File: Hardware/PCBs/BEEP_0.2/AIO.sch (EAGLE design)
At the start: 83 parts, among them IC1 ULN2803ASOP18, IC2 ULN2803ASOP18, IC3 74HC238SSOP, IC4 74HC238SSOP, IC5 TS34119SMD, U2 TB6612FNG, U3 ATXMEGA64D3-AU, X1 MICROMATCH-4, X10 MICROMATCH-10, X3 MICROMATCH-8, X4 MICROMATCH-8, X5 MICROMATCH-8, X8 MICROMATCH-8, X9 MICROMATCH-4

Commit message: add poweroff line to atxmega
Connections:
- removed net N$18: R8.2, S1.S, S1.S1, U$7.G1
- new net POWER_OFF: R8.2, S1.S, S1.S1, U$7.G1, U3.PC7
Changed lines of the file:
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@@
 </segment>
 </net>
-<net name="N$18" class="0">
+<net name="POWER_OFF" class="0">
 <segment>
 <pinref part="R8" gate="G$1" pin="2"/>
@@
 <wire x1="492.76" y1="287.02" x2="492.76" y2="284.48" width="0.1524" layer="91"/>
 <junction x="492.76" y="284.48"/>
+<wire x1="497.84" y1="299.72" x2="502.92" y2="299.72" width="0.1524" layer="91"/>
+<label x="502.92" y="299.72" size="1.778" layer="95" xref="yes"/>
+</segment>
+<segment>
+<pinref part="U3" gate="G$1" pin="PC7"/>
+<wire x1="129.54" y1="96.52" x2="134.62" y2="96.52" width="0.1524" layer="91"/>
+<label x="134.62" y="96.52" size="1.27" layer="95" xref="yes"/>
 </segment>
 </net>

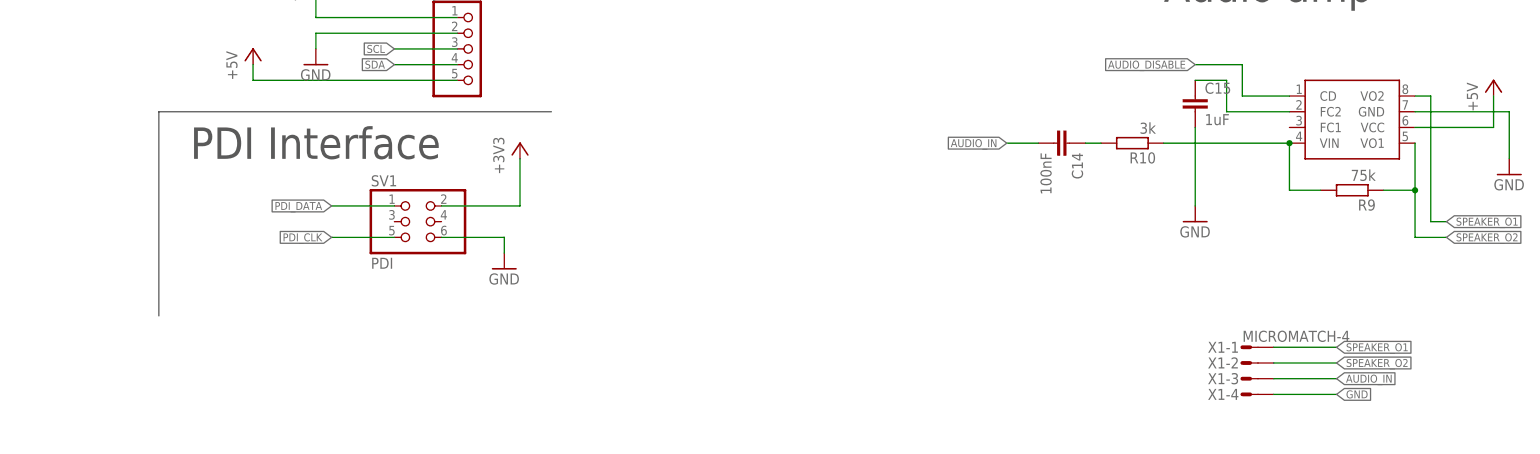
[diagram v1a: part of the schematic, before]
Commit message: move folders try to apply drc from sparkfun (wip) moved audio connetor add slice for camera flexcable
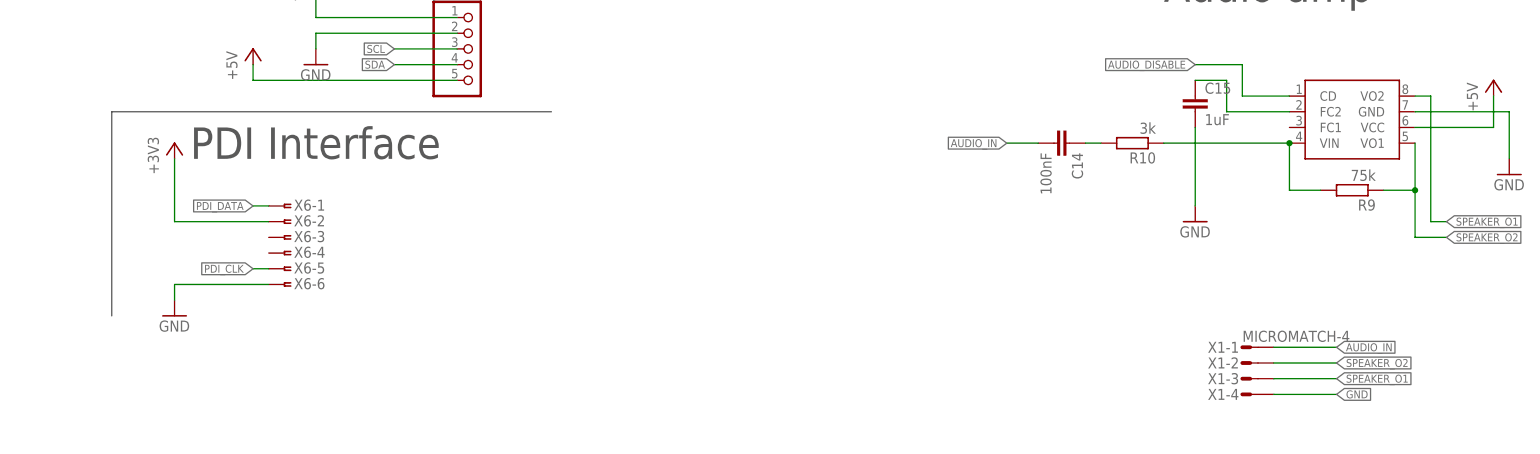
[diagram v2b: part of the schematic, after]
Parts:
- removed SV1: PDI, pinhead:PINHD-2X3
- added X6: (no value), con-amp:FTOP-6
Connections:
- net +3V3: now also X6-2.1; no longer SV1.2
- net AUDIO_IN: now also X1-1.S; no longer X1-3.S
- net GND: now also X6-6.1; no longer SV1.6
- net PDI_CLK: now also X6-5.1; no longer SV1.5
- net PDI_DATA: now also X6-1.1; no longer SV1.1
- net SPEAKER_O1: now also X1-3.S; no longer X1-1.S
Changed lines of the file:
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@@
 <part name="+3V18" library="supply1" deviceset="+3V3" device=""/>
 <part name="+3V19" library="supply1" deviceset="+3V3" device=""/>
-<part name="SV1" library="pinhead" deviceset="PINHD-2X3" device="" value="PDI"/>
-<part name="+3V20" library="supply1" deviceset="+3V3" device=""/>
-<part name="GND37" library="supply1" deviceset="GND" device=""/>
 <part name="+3V21" library="supply1" deviceset="+3V3" device=""/>
 <part name="R34" library="rcl" deviceset="R-EU_" device="R0603" value="10K"/>
@@
 <part name="X1" library="Con-amp-micromatch" deviceset="MICROMATCH-4" device=""/>
 <part name="X2" library="con-amp" deviceset="FSIDE-8" device=""/>
+<part name="X6" library="con-amp" deviceset="FTOP-6" device=""/>
+<part name="+3V8" library="supply1" deviceset="+3V3" device=""/>
+<part name="GND46" library="supply1" deviceset="GND" device=""/>
 </parts>
 <sheets>
@@
 <text x="119.38" y="411.48" size="5.08" layer="97">RGB LEDs &amp; IR distance sensors</text>
 <wire x1="457.2" y1="111.76" x2="457.2" y2="30.48" width="0.1524" layer="97"/>
-<wire x1="269.24" y1="83.82" x2="205.74" y2="83.82" width="0.1524" layer="97"/>
-<wire x1="205.74" y1="83.82" x2="205.74" y2="50.8" width="0.1524" layer="97"/>
+<wire x1="269.24" y1="83.82" x2="198.12" y2="83.82" width="0.1524" layer="97"/>
+<wire x1="198.12" y1="83.82" x2="198.12" y2="50.8" width="0.1524" layer="97"/>
 <text x="210.82" y="76.2" size="5.08" layer="97">PDI Interface</text>
 <wire x1="269.24" y1="127" x2="269.24" y2="124.46" width="0.1524" layer="97"/>
@@
 <instance part="+3V18" gate="G$1" x="215.9" y="187.96"/>
 <instance part="+3V19" gate="G$1" x="220.98" y="187.96"/>
-<instance part="SV1" gate="A" x="246.38" y="66.04"/>
-<instance part="+3V20" gate="G$1" x="264.16" y="78.74"/>
-<instance part="GND37" gate="1" x="261.62" y="58.42"/>
 <instance part="+3V21" gate="G$1" x="86.36" y="182.88"/>
 <instance part="R34" gate="G$1" x="86.36" y="170.18" rot="R270"/>
@@
 <instance part="X2" gate="-7" x="228.6" y="345.44"/>
 <instance part="X2" gate="-8" x="228.6" y="342.9"/>
+<instance part="X6" gate="-1" x="226.06" y="68.58"/>
+<instance part="X6" gate="-2" x="226.06" y="66.04"/>
+<instance part="X6" gate="-3" x="226.06" y="63.5"/>
+<instance part="X6" gate="-4" x="226.06" y="60.96"/>
+<instance part="X6" gate="-5" x="226.06" y="58.42"/>
+<instance part="X6" gate="-6" x="226.06" y="55.88"/>
+<instance part="+3V8" gate="G$1" x="208.28" y="78.74"/>
+<instance part="GND46" gate="1" x="208.28" y="50.8"/>
 </instances>
 <busses>
@@
 <wire x1="238.76" y1="165.1" x2="228.6" y2="165.1" width="0.1524" layer="91"/>
 <wire x1="228.6" y1="165.1" x2="228.6" y2="154.94" width="0.1524" layer="91"/>
-</segment>
-<segment>
-<pinref part="SV1" gate="A" pin="6"/>
-<pinref part="GND37" gate="1" pin="GND"/>
-<wire x1="251.46" y1="63.5" x2="261.62" y2="63.5" width="0.1524" layer="91"/>
-<wire x1="261.62" y1="63.5" x2="261.62" y2="60.96" width="0.1524" layer="91"/>
 </segment>
 <segment>
@@
 <wire x1="386.08" y1="38.1" x2="396.24" y2="38.1" width="0.1524" layer="91"/>
 <label x="396.24" y="38.1" size="1.27" layer="95" xref="yes"/>
+</segment>
+<segment>
+<pinref part="GND46" gate="1" pin="GND"/>
+<wire x1="223.52" y1="55.88" x2="208.28" y2="55.88" width="0.1524" layer="91"/>
+<wire x1="208.28" y1="55.88" x2="208.28" y2="53.34" width="0.1524" layer="91"/>
+<pinref part="X6" gate="-6" pin="1"/>
 </segment>
 </net>
@@
 </segment>
 <segment>
-<pinref part="SV1" gate="A" pin="2"/>
-<pinref part="+3V20" gate="G$1" pin="+3V3"/>
-<wire x1="251.46" y1="68.58" x2="264.16" y2="68.58" width="0.1524" layer="91"/>
-<wire x1="264.16" y1="68.58" x2="264.16" y2="76.2" width="0.1524" layer="91"/>
-</segment>
-<segment>
 <pinref part="R34" gate="G$1" pin="1"/>
 <pinref part="+3V21" gate="G$1" pin="+3V3"/>
@@
 <wire x1="254" y1="99.06" x2="231.14" y2="99.06" width="0.1524" layer="91"/>
 <wire x1="231.14" y1="99.06" x2="231.14" y2="104.14" width="0.1524" layer="91"/>
+</segment>
+<segment>
+<pinref part="+3V8" gate="G$1" pin="+3V3"/>
+<wire x1="223.52" y1="66.04" x2="208.28" y2="66.04" width="0.1524" layer="91"/>
+<wire x1="208.28" y1="66.04" x2="208.28" y2="76.2" width="0.1524" layer="91"/>
+<pinref part="X6" gate="-2" pin="1"/>
 </segment>
 </net>
@@
 <net name="PDI_DATA" class="0">
 <segment>
-<pinref part="SV1" gate="A" pin="1"/>
-<wire x1="243.84" y1="68.58" x2="233.68" y2="68.58" width="0.1524" layer="91"/>
-<label x="233.68" y="68.58" size="1.27" layer="95" rot="R180" xref="yes"/>
-</segment>
-<segment>
 <wire x1="93.98" y1="157.48" x2="78.74" y2="157.48" width="0.1524" layer="91"/>
 <label x="78.74" y="157.48" size="1.27" layer="95" rot="R180" xref="yes"/>
 <pinref part="U3" gate="G$1" pin="PDI"/>
 </segment>
+<segment>
+<label x="220.98" y="68.58" size="1.27" layer="95" rot="R180" xref="yes"/>
+<pinref part="X6" gate="-1" pin="1"/>
+<wire x1="220.98" y1="68.58" x2="223.52" y2="68.58" width="0.1524" layer="91"/>
+</segment>
 </net>
 <net name="PDI_CLK" class="0">
-<segment>
-<pinref part="SV1" gate="A" pin="5"/>
-<wire x1="243.84" y1="63.5" x2="233.68" y2="63.5" width="0.1524" layer="91"/>
-<label x="233.68" y="63.5" size="1.27" layer="95" rot="R180" xref="yes"/>
-</segment>
 <segment>
 <wire x1="93.98" y1="160.02" x2="86.36" y2="160.02" width="0.1524" layer="91"/>
@@
 <junction x="86.36" y="160.02"/>
 <pinref part="U3" gate="G$1" pin="!RESET!/PDI"/>
+</segment>
+<segment>
+<label x="220.98" y="58.42" size="1.27" layer="95" rot="R180" xref="yes"/>
+<pinref part="X6" gate="-5" pin="1"/>
+<wire x1="220.98" y1="58.42" x2="223.52" y2="58.42" width="0.1524" layer="91"/>
 </segment>
 </net>
@@
 </segment>
 <segment>
-<wire x1="386.08" y1="40.64" x2="396.24" y2="40.64" width="0.1524" layer="91"/>
-<pinref part="X1" gate="-3" pin="S"/>
-<label x="396.24" y="40.64" size="1.27" layer="95" xref="yes"/>
+<wire x1="386.08" y1="45.72" x2="396.24" y2="45.72" width="0.1524" layer="91"/>
+<pinref part="X1" gate="-1" pin="S"/>
+<label x="396.24" y="45.72" size="1.27" layer="95" xref="yes"/>
 </segment>
 </net>
@@
 </segment>
 <segment>
-<wire x1="386.08" y1="45.72" x2="396.24" y2="45.72" width="0.1524" layer="91"/>
-<pinref part="X1" gate="-1" pin="S"/>
-<label x="396.24" y="45.72" size="1.27" layer="95" xref="yes"/>
-</segment>
-</net>
+<wire x1="386.08" y1="40.64" x2="396.24" y2="40.64" width="0.1524" layer="91"/>
+<pinref part="X1" gate="-3" pin="S"/>
+<label x="396.24" y="40.64" size="1.27" layer="95" xref="yes"/>
+</segment>
+</net>

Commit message: enhance routing, add external crystal, move components for Raspberry Pi
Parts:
- removed JP12: Step_Down_Conn, pinhead:PINHD-1X3
- removed R32, R33: (no value), rcl:R-EU_R0603
- removed R34: 10K, rcl:R-EU_R0603
- removed R35, R36, R37: 100R, rcl:R-EU_R0603
- removed U$25: GY-81, BEEP:GY-81
- removed U$26: RASPBERRY-PI, BEEP:RASPBERRY-PI
- removed X15: (no value), con-amp:FSIDE-8
- added C16, C17: 22pF, rcl:C-EUC0603
- added Q4, Q5: DMN2075U, BEEP:DMN2075U
- added Q6: 32Mhz, crystal:CRYSTALHC49S
- added R11: 10k, rcl:R-EU_R0603
- added R12: 220R, rcl:R-EU_R0603
- added R13: 390R, rcl:R-EU_R0603
- added R15, R16: (no value), rcl:R-EU_R0603
- added R17: 3k, rcl:R-EU_R0603
- added R18: 75k, rcl:R-EU_R0603
- added X12, X13: MICROMATCH-4, Con-amp-micromatch:MICROMATCH-4
- C10: value 100nF -> 1uF
- C11, C12: value 100nF -> 10uF; device rcl:C-EUC0603 -> rcl:CPOL-EUSMCD
- C13: value 1uF -> 100nF
- C2, C4: value 10uF -> 100nF; device rcl:CPOL-EUSMCD -> rcl:C-EUC0603
- IC1, IC2: value ULN2803ASOP18 -> 74HC238SSOP; device BEEP:ULN2803ASOP18 -> BEEP:74HC238SSOP
- IC3, IC4: value 74HC238SSOP -> ULN2803ASOP18; device BEEP:74HC238SSOP -> BEEP:ULN2803ASOP18
- JP1: value (none) -> Step_Down_Conn; device pinhead:PINHD-1X5 -> pinhead:PINHD-1X3
- LED1: value (none) -> YELLOW
- LED2: value (none) -> RED
- LED3: value (none) -> blue
- R1, R2, R3: value (none) -> 100R
- R10: value 3k -> 10k
- R19: value (none) -> 1K
- R20, R24: value (none) -> 10k
- R21: value (none) -> 100k
- R22, R23, R25, R26, R27, R28, R29, R30: device rcl:R-EU_R0603 -> rcl:R-EU_R0805
- R31: value (none) -> 0R
- R4, R5: value 10K -> (none); device rcl:R-EU_R0603 -> rcl:R-EU_R0805
- R6: value 10k -> (none); device rcl:R-EU_R0603 -> rcl:R-EU_R0805
- R7: value 100k -> 10K
- R8: value 10k -> (none)
- R9: value 75k -> (none)
- S1: value (none) -> On / Off
- U$5: value DMN2075U -> GY-81; device BEEP:DMN2075U -> BEEP:GY-81
- U$7: value DMC3028LSD -> RASPBERRY-PI; device BEEP:DMC3028LSD -> BEEP:RASPBERRY-PI
- U$8: value DMN2075U -> DMC3028LSD; device BEEP:DMN2075U -> BEEP:DMC3028LSD
- X1: value MICROMATCH-4 -> Sens1; device Con-amp-micromatch:MICROMATCH-4 -> con-amp:FSIDE-8
- X10: value MICROMATCH-10 -> exp header; device Con-amp-micromatch:MICROMATCH-10 -> con-amp:FTOP-6
- X11: value (none) -> MICROMATCH-10; device con-amp:FSIDE-8 -> Con-amp-micromatch:MICROMATCH-10
- X2: value (none) -> Sens2
- X5: value MICROMATCH-8 -> PDI interface (ISP); device Con-amp-micromatch:MICROMATCH-8 -> con-amp:FTOP-6
- X6: value (none) -> Sens5; device con-amp:FTOP-6 -> con-amp:FSIDE-8
- X7: value (none) -> Sens6
- X9: value MICROMATCH-4 -> MICROMATCH-8; device Con-amp-micromatch:MICROMATCH-4 -> Con-amp-micromatch:MICROMATCH-8
- renumbered JP13 to JP2, LED10 to LED1, LED11 to LED3, LED9 to LED2, R41 to R14, R42 to R19, U$1 to Q3, U$2 to Q2, U$21 to U$9, U$22 to U$11, U$23 to U$10, U$24 to U$12, U$3 to Q1, U3 to U1, X16 to X7
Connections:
- new net N$14: C17.2, Q6.1, U1.PR1
- new net N$18: C16.2, Q6.2, U1.PR0
- net +3V3: now also C11.-, C13.2, C2.2, C3.2, C4.2, IC1.G1, IC1.VCC, IC2.G1, IC2.VCC, R10.1, R11.1, R7.1, R8.1, U$5.3V3, U$5.VCC_IN, U$7.+3V3, X10-1.1, X11-10.S, X5-2.1; no longer C10.2, C11.2, C12.2, C2.-, C9.2, IC3.G1, IC3.VCC, IC4.G1, IC4.VCC, JP1.1, R32.1, R33.1, R34.1, R5.1, U$25.3V3, U$25.VCC_IN, U$26.3V3, X10-10.S, X6-2.1
- net +5V: now also JP1.3, Q5.D, R26.2, R29.2, R30.2, U$7.+5V, X1-1.1, X10-5.1, X6-1.1, X9-8.S; no longer JP1.5, JP12.3, R21.2, R23.2, R27.2, U$26.5V, U$8.D, X11-1.1, X15-1.1, X5-8.S
- net +7V: now also C12.-, C14.2, JP1.1, R15.1, R24.1, R31.2, U$8.D2; no longer C3.2, C4.-, JP12.1, R28.1, R8.1, U$7.D2
- net ADISTANCE_0: now also X3-7.S; no longer X4-7.S
- net ADISTANCE_1: now also X1-2.1; no longer X11-2.1
- net ADISTANCE_2: now also X2-2.1; no longer X15-2.1
- net ADISTANCE_3: now also X4-7.S; no longer X3-7.S
- net ADISTANCE_4: now also X8-7.S; no longer X5-7.S
- net ADISTANCE_5: now also X6-2.1; no longer X2-2.1
- net ADISTANCE_7: now also X9-7.S; no longer X8-7.S
- net AUDIO_IN: now also C9.2, X13-1.S; no longer C14.2, X1-1.S
- net BATT_GND: now also Q4.D; no longer U$5.D
- net BATT_U: now also R20.1, R31.1, U$8.S2; no longer R6.1, U$7.S2
- net BATT_VOLTAGE: now also R15.2, R16.1; no longer R28.2, R29.1
- net BATT_WARN_0: now also R12.1; no longer R31.1
- net BATT_WARN_1: now also R13.1; no longer R30.1
- net COLOR_DIODE_1: now also X11-4.S; no longer X10-4.S
- net COLOR_DIODE_2: now also X11-3.S; no longer X10-3.S
- net COLOR_FREQ_OUT: now also X11-7.S; no longer X10-7.S
- net COLOR_SENSOR_1: now also X11-2.S; no longer X10-2.S
- net COLOR_SENSOR_2: now also X11-6.S; no longer X10-6.S
- net COLOR_SENSOR_3: now also X11-5.S; no longer X10-5.S
- net COLOR_SENSOR_PWM_LED: now also Q5.G; no longer U$8.G
- net ENCODER_L1: now also R22.2; no longer R20.2
- net ENCODER_L2: now also R27.2; no longer R22.2
- net ENCODER_R1: now also R23.2; no longer R24.2
- net ENCODER_R2: now also R28.2; no longer R26.2
- net GND: now also C10.2, C11.+, C12.+, C13.1, C14.1, C16.1, C17.1, C2.1, C4.1, IC1.G2A, IC1.G2B, IC2.G2A, IC2.G2B, Q4.S, R16.2, R23.1, R27.1, R28.1, R9.2, U$5.GND, U$7.GND, U$8.S1, X1-3.1, X10-2.1, X11-8.S, X13-4.S, X5-6.1, X6-3.1, X9-6.S; no longer C10.1, C11.1, C12.1, C13.2, C2.+, C4.+, C9.1, IC3.G2A, IC3.G2B, IC4.G2A, IC4.G2B, JP12.2, R20.1, R24.1, R26.1, R29.2, R4.2, U$25.GND, U$26.GND, U$5.S, U$7.S1, X1-4.S, X10-8.S, X11-3.1, X15-3.1, X5-6.S, X6-6.1
- net IR_LED_K0: now also IC2.Y0, IC4.I1; no longer IC2.I1, IC3.Y0
- net IR_LED_K0_OUT: now also IC4.O1, X3-5.S; no longer IC2.O1, X4-5.S
- net IR_LED_K1: now also IC2.Y1, IC4.I2; no longer IC2.I2, IC3.Y1
- net IR_LED_K1_OUT: now also IC4.O2, X1-4.1; no longer IC2.O2, X11-4.1
- net IR_LED_K2_OUT: now also IC4.O3, X2-4.1; no longer IC2.O3, X15-4.1
- net IR_LED_K3_OUT: now also IC4.O4, X4-5.S; no longer IC2.O4, X3-5.S
- net IR_LED_K4_OUT: now also IC4.O6, X8-5.S; no longer IC2.O6, X5-5.S
- net IR_LED_K5_OUT: now also IC4.O7, X6-4.1; no longer IC2.O7, X2-4.1
- net IR_LED_K6_OUT: now also IC4.O8; no longer IC2.O8
- net IR_LED_K7_OUT: now also IC4.O5, X9-5.S; no longer IC2.O5, X8-5.S
- net IR_LED_MK0: now also IC2.A; no longer IC3.A
- net IR_LED_MK1: now also IC2.B; no longer IC3.B
- net IR_LED_MK2: now also IC2.C; no longer IC3.C
- net LED_A0: now also R1.1; no longer R35.1
- net LED_A0_OUT: now also R6.2, X1-8.1, X6-8.1, X9-1.S; no longer R3.2, X11-8.1, X15-8.1, X5-1.S
- net LED_A1: now also R2.1; no longer R36.1
- net LED_A1_OUT: now also R5.2, X1-7.1, X6-7.1, X9-2.S; no longer R2.2, X11-7.1, X15-7.1, X5-2.S
- net LED_A2: now also R3.1; no longer R37.1
- net LED_A2_OUT: now also R4.2, X1-6.1, X6-6.1, X9-3.S; no longer R1.2, X11-6.1, X15-6.1, X5-3.S
- net LED_K0_OUT: now also IC3.O1, X3-4.S; no longer IC1.O1, X4-4.S
- net LED_K1_OUT: now also IC3.O2, X1-5.1; no longer IC1.O2, X11-5.1
- net LED_K2_OUT: now also IC3.O3, X2-5.1; no longer IC1.O3, X15-5.1
- net LED_K3_OUT: now also IC3.O4, X4-4.S; no longer IC1.O4, X3-4.S
- net LED_K4_OUT: now also IC3.O5, X8-4.S; no longer IC1.O5, X5-4.S
- net LED_K5_OUT: now also IC3.O6, X6-5.1; no longer IC1.O6, X2-5.1
- net LED_K6_OUT: now also IC3.O7; no longer IC1.O7
- net LED_K7_OUT: now also IC3.O8, X9-4.S; no longer IC1.O8, X8-4.S
- net MOTOR_A_OUT1: now also X12-1.S; no longer X9-1.S
- net MOTOR_A_OUT2: now also X12-2.S; no longer X9-2.S
- net MOTOR_B_OUT1: now also X12-4.S; no longer X9-4.S
- net MOTOR_B_OUT2: now also X12-3.S; no longer X9-3.S
- net N$1: now also R4.1; no longer R1.1
- net N$10: now also IC2.Y5, IC4.I6; no longer IC2.I6, IC3.Y5
- net N$11: now also R29.1; no longer R23.1
- net N$12: now also IC2.Y6, IC4.I7; no longer IC2.I7, IC3.Y6
- net N$13: now also IC2.Y7, IC4.I8; no longer IC2.I8, IC3.Y7
- net N$15: now also R17.1, R18.2; no longer R10.1, R9.2
- net N$16: now also C15.1, R21.2; no longer C13.1, R7.2
- net N$17: now also C9.1, R17.2; no longer C14.1, R10.2
- net N$2: now also R5.1; no longer R2.1
- net N$20: now also R26.1; no longer R25.1
- net N$21: now also IC1.Y0, IC3.I1; no longer IC1.I1, IC4.Y0
- net N$22: now also R20.2, R21.1, U$8.D1, U$8.G2; no longer R6.2, R7.1, U$7.D1, U$7.G2
- net N$23: now also R25.1; no longer R21.1
- net N$24: now also IC1.Y1, IC3.I2; no longer IC1.I2, IC4.Y1
- net N$26: now also R30.1; no longer R27.1
- net N$27: now also IC1.Y2, IC3.I3; no longer IC1.I3, IC4.Y2
- net N$28: now also IC1.Y3, IC3.I4; no longer IC1.I4, IC4.Y3
- net N$29: now also R13.2; no longer R30.2
- net N$3: now also R6.1; no longer R3.1
- net N$30: now also IC1.Y4, IC3.I5; no longer IC1.I5, IC4.Y4
- net N$31: now also IC1.Y5, IC3.I6; no longer IC1.I6, IC4.Y5
- net N$32: now also R12.2; no longer R31.2
- net N$33: now also IC1.Y6, IC3.I7; no longer IC1.I7, IC4.Y6
- net N$34: now also IC1.Y7, IC3.I8; no longer IC1.I8, IC4.Y7
- net N$36: now also C10.1; no longer C15.1
- net N$38: now also R1.2; no longer R35.2
- net N$39: now also R2.2; no longer R36.2
- net N$4: now also R8.2, R9.1; no longer R4.1, R5.2
- net N$40: now also R3.2; no longer R37.2
- net N$5: now also Q5.S, X11-9.S; no longer U$8.S, X10-9.S
- net N$6: now also IC2.Y2, IC4.I3; no longer IC2.I3, IC3.Y2
- net N$7: now also IC2.Y3, IC4.I4; no longer IC2.I4, IC3.Y3
- net N$8: now also Q4.G; no longer U$5.G
- net N$9: now also IC2.Y4, IC4.I5; no longer IC2.I5, IC3.Y4
- net PDI_CLK: now also R7.2, X5-5.1; no longer R34.2, X6-5.1
- net PDI_DATA: now also X5-1.1; no longer X6-1.1
- net POWER_OFF: now also R24.2, U$8.G1; no longer R8.2, U$7.G1
- net RGB_LED_MK0: now also IC1.A; no longer IC4.A
- net RGB_LED_MK1: now also IC1.B; no longer IC4.B
- net RGB_LED_MK2: now also IC1.C; no longer IC4.C
- net RPI_RX: now also U$7.GPIO_15; no longer U$26.GPIO_15
- net RPI_TX: now also U$7.GPIO_14; no longer U$26.GPIO_14
- net SCL: now also R11.2, U$5.SCL, U$7.GPIO_1, X10-3.1; no longer JP1.3, R32.2, U$25.SCL, U$26.GPIO_1
- net SDA: now also R10.2, U$5.SDA, U$7.GPIO_0, X10-4.1; no longer JP1.4, R33.2, U$25.SDA, U$26.GPIO_0
- net SPEAKER_O1: now also X13-3.S; no longer X1-3.S
- net SPEAKER_O2: now also R18.1, X13-2.S; no longer R9.1, X1-2.S
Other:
- note added: "Brücke falls Schaltung versagt ;)"
- note added: "Optional"
- note added: "Optional für alte XMega revisionen (siehe Errata)"
- note added: "TODO: *3M Stecker *Stecker codierung? *Spannungsteiler berechnen, ADC nachlesen *Silkscreen sortieren?"
- moved on the sheet: C1, C10, C13, C14, C15, C3, C5, C7, C8, C9, R1, R10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

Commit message: Use PORTC for TWI, bcause of really annoying errata that states that TWI on PORT E is unusable for Revisions prior of I. damn errata!!!
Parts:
- added R32: 100R, rcl:R-EU_R0603
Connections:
- new net N$25: Q5.G, R32.2
- net COLOR_SENSOR_PWM_LED: now also R32.1, U1.PE3; no longer Q5.G, U1.PC3
- net LED_A0: now also U1.PE0; no longer U1.PC0
- net LED_A1: now also U1.PE1; no longer U1.PC1
- net LED_A2: now also U1.PE2; no longer U1.PC2
- net MOTOR_A_PWM: now also U1.PC3; no longer U1.PE3
- net MOTOR_B_PWM: now also U1.PC2; no longer U1.PE2
- net SCL: now also U1.PC1; no longer U1.PE1
- net SDA: now also U1.PC0; no longer U1.PE0
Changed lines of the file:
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@@
 <part name="GND37" library="supply1" deviceset="GND" device=""/>
 <part name="R31" library="rcl" deviceset="R-EU_" device="R0603" value="0R"/>
+<part name="R32" library="rcl" deviceset="R-EU_" device="R0603" value="100R"/>
 </parts>
 <sheets>
@@
 <instance part="GND37" gate="1" x="60.96" y="116.84"/>
 <instance part="R31" gate="G$1" x="525.78" y="340.36"/>
+<instance part="R32" gate="G$1" x="213.36" y="132.08"/>
 </instances>
 <busses>
@@
 </segment>
 <segment>
-<label x="88.9" y="109.22" size="1.27" layer="95" rot="R180" xref="yes"/>
-<pinref part="U1" gate="G$1" pin="PE2"/>
-<wire x1="93.98" y1="109.22" x2="88.9" y2="109.22" width="0.1524" layer="91"/>
+<wire x1="129.54" y1="109.22" x2="134.62" y2="109.22" width="0.1524" layer="91" style="longdash"/>
+<label x="134.62" y="109.22" size="1.27" layer="95" xref="yes"/>
+<pinref part="U1" gate="G$1" pin="PC2"/>
 </segment>
 </net>
@@
 </segment>
 <segment>
-<label x="88.9" y="106.68" size="1.27" layer="95" rot="R180" xref="yes"/>
-<pinref part="U1" gate="G$1" pin="PE3"/>
-<wire x1="93.98" y1="106.68" x2="88.9" y2="106.68" width="0.1524" layer="91"/>
+<wire x1="129.54" y1="106.68" x2="134.62" y2="106.68" width="0.1524" layer="91" style="longdash"/>
+<label x="134.62" y="106.68" size="1.27" layer="95" xref="yes"/>
+<pinref part="U1" gate="G$1" pin="PC3"/>
 </segment>
 </net>
@@
 </segment>
 <segment>
-<pinref part="U1" gate="G$1" pin="PE1"/>
-<wire x1="93.98" y1="111.76" x2="88.9" y2="111.76" width="0.1524" layer="91"/>
-<label x="88.9" y="111.76" size="1.27" layer="95" rot="R180" xref="yes"/>
-</segment>
-<segment>
 <wire x1="241.3" y1="93.98" x2="228.6" y2="93.98" width="0.1524" layer="91"/>
 <label x="228.6" y="93.98" size="1.27" layer="95" rot="R180" xref="yes"/>
 <pinref part="X10" gate="-3" pin="1"/>
+</segment>
+<segment>
+<wire x1="129.54" y1="111.76" x2="134.62" y2="111.76" width="0.1524" layer="91" style="longdash"/>
+<label x="134.62" y="111.76" size="1.27" layer="95" xref="yes"/>
+<pinref part="U1" gate="G$1" pin="PC1"/>
 </segment>
 </net>
@@
 </segment>
 <segment>
-<pinref part="U1" gate="G$1" pin="PE0"/>
-<wire x1="93.98" y1="114.3" x2="88.9" y2="114.3" width="0.1524" layer="91"/>
-<label x="88.9" y="114.3" size="1.27" layer="95" rot="R180" xref="yes"/>
-</segment>
-<segment>
 <wire x1="241.3" y1="91.44" x2="228.6" y2="91.44" width="0.1524" layer="91"/>
 <label x="228.6" y="91.44" size="1.27" layer="95" rot="R180" xref="yes"/>
 <pinref part="X10" gate="-4" pin="1"/>
+</segment>
+<segment>
+<wire x1="129.54" y1="114.3" x2="134.62" y2="114.3" width="0.1524" layer="91" style="longdash"/>
+<label x="134.62" y="114.3" size="1.27" layer="95" xref="yes"/>
+<pinref part="U1" gate="G$1" pin="PC0"/>
 </segment>
 </net>
@@
 </segment>
 <segment>
-<wire x1="129.54" y1="109.22" x2="134.62" y2="109.22" width="0.1524" layer="91" style="longdash"/>
-<label x="134.62" y="109.22" size="1.27" layer="95" xref="yes"/>
-<pinref part="U1" gate="G$1" pin="PC2"/>
+<label x="88.9" y="109.22" size="1.27" layer="95" rot="R180" xref="yes"/>
+<pinref part="U1" gate="G$1" pin="PE2"/>
+<wire x1="93.98" y1="109.22" x2="88.9" y2="109.22" width="0.1524" layer="91"/>
 </segment>
 </net>
@@
 </segment>
 <segment>
-<wire x1="129.54" y1="111.76" x2="134.62" y2="111.76" width="0.1524" layer="91" style="longdash"/>
-<label x="134.62" y="111.76" size="1.27" layer="95" xref="yes"/>
-<pinref part="U1" gate="G$1" pin="PC1"/>
+<pinref part="U1" gate="G$1" pin="PE1"/>
+<wire x1="93.98" y1="111.76" x2="88.9" y2="111.76" width="0.1524" layer="91"/>
+<label x="88.9" y="111.76" size="1.27" layer="95" rot="R180" xref="yes"/>
 </segment>
 </net>
@@
 </segment>
 <segment>
-<wire x1="129.54" y1="114.3" x2="134.62" y2="114.3" width="0.1524" layer="91" style="longdash"/>
-<label x="134.62" y="114.3" size="1.27" layer="95" xref="yes"/>
-<pinref part="U1" gate="G$1" pin="PC0"/>
+<pinref part="U1" gate="G$1" pin="PE0"/>
+<wire x1="93.98" y1="114.3" x2="88.9" y2="114.3" width="0.1524" layer="91"/>
+<label x="88.9" y="114.3" size="1.27" layer="95" rot="R180" xref="yes"/>
 </segment>
 </net>
@@
 <net name="COLOR_SENSOR_PWM_LED" class="0">
 <segment>
-<pinref part="Q5" gate="G$1" pin="G"/>
-<wire x1="220.98" y1="132.08" x2="218.44" y2="132.08" width="0.1524" layer="91"/>
-<label x="218.44" y="132.08" size="1.27" layer="95" rot="R180" xref="yes"/>
-</segment>
-<segment>
-<wire x1="129.54" y1="106.68" x2="134.62" y2="106.68" width="0.1524" layer="91" style="longdash"/>
-<label x="134.62" y="106.68" size="1.27" layer="95" xref="yes"/>
-<pinref part="U1" gate="G$1" pin="PC3"/>
+<label x="200.66" y="132.08" size="1.27" layer="95" rot="R180" xref="yes"/>
+<wire x1="208.28" y1="132.08" x2="200.66" y2="132.08" width="0.1524" layer="91"/>
+<pinref part="R32" gate="G$1" pin="1"/>
+</segment>
+<segment>
+<label x="88.9" y="106.68" size="1.27" layer="95" rot="R180" xref="yes"/>
+<pinref part="U1" gate="G$1" pin="PE3"/>
+<wire x1="93.98" y1="106.68" x2="88.9" y2="106.68" width="0.1524" layer="91"/>
 </segment>
 </net>
@@
 </segment>
 </net>
+<net name="N$25" class="0">
+<segment>
+<pinref part="Q5" gate="G$1" pin="G"/>
+<wire x1="220.98" y1="132.08" x2="218.44" y2="132.08" width="0.1524" layer="91"/>
+<pinref part="R32" gate="G$1" pin="2"/>
+</segment>
+</net>
